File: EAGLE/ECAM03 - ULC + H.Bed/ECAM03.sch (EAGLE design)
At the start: 45 parts, among them J1 MODULAR TOOL, J2 FAN1, J3 FAN2, J4 FAN3, J5 S4B-PH-SM4, J6 SSR, J7 RINGLIGHT, J8 FTDI, J9 SPI, Q2 16MHz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

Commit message: BOMs complete for all FPD boards
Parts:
- C12: PARTNO (none) -> GRM188R61C106MA73D
- D1: PARTNO (none) -> B340A-13-F
- J2, J3, J4: PARTNO (none) -> 22232031
- J5: value S4B-PH-SM4 -> B4B-PH-SM4; PARTNO S4B-PH-SM4-TB(LF)(SN) -> B4B-PH-SM4-TB(LF)(SN)
- J6: PARTNO (none) -> 68000-102HLF
- J7: PARTNO (none) -> B5B-PH-SM4-TB(LF)(SN)
- J9: PARTNO (none) -> 67996-206HLF
- L1: PARTNO (none) -> BRL1608T6R8M
- R1: PARTNO (none) -> RC0603FR-0710KL
- R12: PARTNO (none) -> RC0603FR-0790K9L
- R15, R16: PARTNO (none) -> RC0603JR-070RL
- R6: PARTNO (none) -> RC0603FR-074K99L
- R7: PARTNO (none) -> RC1206FR-0710RL
- TB1: PARTNO (none) -> OSTTH020160
- U$1: PARTNO (none) -> *
- U3: PARTNO (none) -> MCP4725A0T-E/CH
- U4: PARTNO (none) -> MAX31855KASA+
- U5: PARTNO (none) -> NTR4003NT3G
- U6: PARTNO (none) -> SN74LVC1G02DBVR
- U8: PARTNO (none) -> AP3032KTR-G1

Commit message: BOMs finished, inventory sheet created.
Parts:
- R12: value 90K -> 90K9
- R2: PARTNO RC0603FR-07100RL -> RC0603FR-07120RL
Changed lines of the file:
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@@
 <part name="P+2" library="supply1" deviceset="+5V" device=""/>
 <part name="R2" library="TinWhiskers" deviceset="CPL-RES-0603-120-0.1W" device="" value="120R">
-<attribute name="PARTNO" value="RC0603FR-07100RL"/>
+<attribute name="PARTNO" value="RC0603FR-07120RL"/>
 </part>
 <part name="R3" library="TinWhiskers" deviceset="CPL-RES-0603-1K-0.1W" device="" value="1K">
@@
 <attribute name="PARTNO" value="RC1206FR-0710RL"/>
 </part>
-<part name="R12" library="TinWhiskers" deviceset="CPL-RES-0603-90K-0.1W" device="" value="90K">
+<part name="R12" library="TinWhiskers" deviceset="CPL-RES-0603-90K-0.1W" device="" value="90K9">
 <attribute name="PARTNO" value="RC0603FR-0790K9L"/>
 </part>

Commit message: Added decoupling caps to EFD01, ECAM02, rearranged parts for better fit, increased power trace width, updated BOM and database.
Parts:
- added C1, C10, C11, C2, C3, C9: 0.1uF, TinWhiskers:CPL-CAP-X5R-0603-0.1UF-35V
- U5: device TinWhiskers:CPL-MOSFET-NCH-SOT23 -> TinWhiskers:CPL-MOSFET-NCH-SOT23NTR4003N
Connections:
- net +3V3: now also C2.2
- net +5V: now also C1.2, C10.2, C11.2, C3.2, C9.2
- net GND: now also C1.1, C10.1, C11.1, C2.1, C3.1, C9.1; no longer U2.TAB
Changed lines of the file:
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@@
 <part name="SUPPLY10" library="TinWhiskers" deviceset="GND" device=""/>
 <part name="P+7" library="supply1" deviceset="+5V" device=""/>
-<part name="SUPPLY11" library="TinWhiskers" deviceset="GND" device=""/>
 <part name="SUPPLY12" library="TinWhiskers" deviceset="GND" device=""/>
 <part name="U1" library="TinWhiskers" deviceset="SP3485" device="">
@@
 <attribute name="PARTNO" value="22232031"/>
 </part>
-<part name="U5" library="TinWhiskers" deviceset="CPL-MOSFET-NCH-SOT23" device="" value="NTR4003NT3G">
+<part name="U5" library="TinWhiskers" deviceset="CPL-MOSFET-NCH-SOT23" device="NTR4003N" value="NTR4003NT3G">
 <attribute name="PARTNO" value="NTR4003NT3G"/>
 </part>
@@
 </part>
 <part name="SUPPLY5" library="TinWhiskers" deviceset="GND" device=""/>
+<part name="C1" library="TinWhiskers" deviceset="CPL-CAP-X5R-0603-0.1UF-35V" device="" value="0.1uF"/>
+<part name="SUPPLY19" library="TinWhiskers" deviceset="GND" device=""/>
+<part name="C2" library="TinWhiskers" deviceset="CPL-CAP-X5R-0603-0.1UF-35V" device="" value="0.1uF"/>
+<part name="+3V5" library="supply1" deviceset="+3V3" device=""/>
+<part name="SUPPLY20" library="TinWhiskers" deviceset="GND" device=""/>
+<part name="C3" library="TinWhiskers" deviceset="CPL-CAP-X5R-0603-0.1UF-35V" device="" value="0.1uF"/>
+<part name="SUPPLY21" library="TinWhiskers" deviceset="GND" device=""/>
+<part name="P+17" library="supply1" deviceset="+5V" device=""/>
+<part name="C9" library="TinWhiskers" deviceset="CPL-CAP-X5R-0603-0.1UF-35V" device="" value="0.1uF"/>
+<part name="SUPPLY24" library="TinWhiskers" deviceset="GND" device=""/>
+<part name="P+18" library="supply1" deviceset="+5V" device=""/>
+<part name="C10" library="TinWhiskers" deviceset="CPL-CAP-X5R-0603-0.1UF-35V" device="" value="0.1uF"/>
+<part name="SUPPLY25" library="TinWhiskers" deviceset="GND" device=""/>
+<part name="P+19" library="supply1" deviceset="+5V" device=""/>
+<part name="C11" library="TinWhiskers" deviceset="CPL-CAP-X5R-0603-0.1UF-35V" device="" value="0.1uF"/>
+<part name="SUPPLY28" library="TinWhiskers" deviceset="GND" device=""/>
+<part name="P+20" library="supply1" deviceset="+5V" device=""/>
 </parts>
 <sheets>
@@
 <attribute name="VALUE" x="355.6" y="236.22" size="1.778" layer="96"/>
 </instance>
-<instance part="SUPPLY11" gate="GND" x="320.04" y="175.26"/>
 <instance part="SUPPLY12" gate="GND" x="347.98" y="175.26"/>
 <instance part="U1" gate="G$1" x="210.82" y="116.84" smashed="yes">
@@
 <attribute name="PARTNO" x="233.68" y="101.6" size="2.54" layer="96" ratio="10" display="off"/>
 </instance>
-<instance part="+3V2" gate="G$1" x="233.68" y="142.24"/>
-<instance part="+3V3" gate="G$1" x="226.06" y="142.24"/>
+<instance part="+3V2" gate="G$1" x="233.68" y="142.24" smashed="yes">
+<attribute name="VALUE" x="231.14" y="142.24" size="1.778" layer="96"/>
+</instance>
+<instance part="+3V3" gate="G$1" x="226.06" y="142.24" smashed="yes">
+<attribute name="VALUE" x="223.52" y="142.24" size="1.778" layer="96"/>
+</instance>
 <instance part="SUPPLY2" gate="GND" x="233.68" y="91.44"/>
 <instance part="SUPPLY3" gate="GND" x="226.06" y="91.44"/>
@@
 <instance part="SUPPLY5" gate="GND" x="132.08" y="38.1" smashed="yes">
 <attribute name="VALUE" x="130.175" y="34.925" size="1.778" layer="96"/>
+</instance>
+<instance part="C1" gate="G$1" x="279.4" y="220.98" smashed="yes" rot="R90">
+<attribute name="NAME" x="279.019" y="214.884" size="1.778" layer="95" rot="R90"/>
+<attribute name="VALUE" x="281.559" y="211.582" size="1.778" layer="96" rot="R90"/>
+</instance>
+<instance part="SUPPLY19" gate="GND" x="279.4" y="210.82"/>
+<instance part="C2" gate="G$1" x="195.58" y="104.14" smashed="yes" rot="R90">
+<attribute name="NAME" x="195.199" y="98.044" size="1.778" layer="95" rot="R90"/>
+<attribute name="VALUE" x="197.739" y="94.742" size="1.778" layer="96" rot="R90"/>
+</instance>
+<instance part="+3V5" gate="G$1" x="195.58" y="111.76" smashed="yes">
+<attribute name="VALUE" x="193.04" y="111.76" size="1.778" layer="96"/>
+</instance>
+<instance part="SUPPLY20" gate="GND" x="195.58" y="93.98"/>
+<instance part="C3" gate="G$1" x="15.24" y="55.88" smashed="yes" rot="R90">
+<attribute name="NAME" x="14.859" y="49.784" size="1.778" layer="95" rot="R90"/>
+<attribute name="VALUE" x="17.399" y="46.482" size="1.778" layer="96" rot="R90"/>
+</instance>
+<instance part="SUPPLY21" gate="GND" x="15.24" y="45.72"/>
+<instance part="P+17" gate="1" x="15.24" y="63.5" smashed="yes">
+<attribute name="VALUE" x="12.7" y="63.5" size="1.778" layer="96"/>
+</instance>
+<instance part="C9" gate="G$1" x="81.28" y="55.88" smashed="yes" rot="R90">
+<attribute name="NAME" x="80.899" y="49.784" size="1.778" layer="95" rot="R90"/>
+<attribute name="VALUE" x="83.439" y="46.482" size="1.778" layer="96" rot="R90"/>
+</instance>
+<instance part="SUPPLY24" gate="GND" x="81.28" y="45.72"/>
+<instance part="P+18" gate="1" x="81.28" y="63.5" smashed="yes">
+<attribute name="VALUE" x="78.74" y="63.5" size="1.778" layer="96"/>
+</instance>
+<instance part="C10" gate="G$1" x="193.04" y="58.42" smashed="yes" rot="R90">
+<attribute name="NAME" x="192.659" y="51.308" size="1.778" layer="95" rot="R90"/>
+<attribute name="VALUE" x="195.199" y="49.022" size="1.778" layer="96" rot="R90"/>
+</instance>
+<instance part="SUPPLY25" gate="GND" x="193.04" y="48.26"/>
+<instance part="P+19" gate="1" x="193.04" y="66.04" smashed="yes">
+<attribute name="VALUE" x="190.5" y="66.04" size="1.778" layer="96"/>
+</instance>
+<instance part="C11" gate="G$1" x="279.4" y="50.8" smashed="yes" rot="R90">
+<attribute name="NAME" x="279.019" y="43.942" size="1.778" layer="95" rot="R90"/>
+<attribute name="VALUE" x="281.559" y="41.402" size="1.778" layer="96" rot="R90"/>
+</instance>
+<instance part="SUPPLY28" gate="GND" x="279.4" y="40.64"/>
+<instance part="P+20" gate="1" x="279.4" y="58.42" smashed="yes">
+<attribute name="VALUE" x="276.86" y="58.42" size="1.778" layer="96"/>
 </instance>
 </instances>
@@
 </segment>
 <segment>
-<pinref part="U2" gate="G$1" pin="TAB"/>
-<wire x1="322.58" y1="180.34" x2="320.04" y2="180.34" width="0.1524" layer="91"/>
-<wire x1="320.04" y1="180.34" x2="320.04" y2="177.8" width="0.1524" layer="91"/>
-<pinref part="SUPPLY11" gate="GND" pin="GND"/>
-</segment>
-<segment>
 <wire x1="261.62" y1="119.38" x2="259.08" y2="119.38" width="0.1524" layer="91"/>
 <wire x1="259.08" y1="119.38" x2="259.08" y2="106.68" width="0.1524" layer="91"/>
@@
 <wire x1="119.38" y1="55.88" x2="132.08" y2="55.88" width="0.1524" layer="91"/>
 <wire x1="132.08" y1="55.88" x2="132.08" y2="40.64" width="0.1524" layer="91"/>
+</segment>
+<segment>
+<pinref part="C1" gate="G$1" pin="1"/>
+<pinref part="SUPPLY19" gate="GND" pin="GND"/>
+<wire x1="279.4" y1="215.9" x2="279.4" y2="213.36" width="0.1524" layer="91"/>
+</segment>
+<segment>
+<pinref part="C2" gate="G$1" pin="1"/>
+<pinref part="SUPPLY20" gate="GND" pin="GND"/>
+<wire x1="195.58" y1="99.06" x2="195.58" y2="96.52" width="0.1524" layer="91"/>
+</segment>
+<segment>
+<pinref part="C3" gate="G$1" pin="1"/>
+<pinref part="SUPPLY21" gate="GND" pin="GND"/>
+<wire x1="15.24" y1="50.8" x2="15.24" y2="48.26" width="0.1524" layer="91"/>
+</segment>
+<segment>
+<pinref part="C9" gate="G$1" pin="1"/>
+<pinref part="SUPPLY24" gate="GND" pin="GND"/>
+<wire x1="81.28" y1="50.8" x2="81.28" y2="48.26" width="0.1524" layer="91"/>
+</segment>
+<segment>
+<pinref part="C10" gate="G$1" pin="1"/>
+<pinref part="SUPPLY25" gate="GND" pin="GND"/>
+<wire x1="193.04" y1="53.34" x2="193.04" y2="50.8" width="0.1524" layer="91"/>
+</segment>
+<segment>
+<pinref part="C11" gate="G$1" pin="1"/>
+<pinref part="SUPPLY28" gate="GND" pin="GND"/>
+<wire x1="279.4" y1="45.72" x2="279.4" y2="43.18" width="0.1524" layer="91"/>
 </segment>
 </net>
@@
 <wire x1="299.72" y1="226.06" x2="297.18" y2="226.06" width="0.1524" layer="91"/>
 <wire x1="297.18" y1="226.06" x2="297.18" y2="228.6" width="0.1524" layer="91"/>
+<pinref part="C1" gate="G$1" pin="2"/>
+<wire x1="297.18" y1="226.06" x2="279.4" y2="226.06" width="0.1524" layer="91"/>
+<wire x1="279.4" y1="226.06" x2="279.4" y2="223.52" width="0.1524" layer="91"/>
+<junction x="297.18" y="226.06"/>
 </segment>
 <segment>
@@
 <wire x1="149.86" y1="200.66" x2="149.86" y2="203.2" width="0.1524" layer="91"/>
 <pinref part="P+16" gate="1" pin="+5V"/>
+</segment>
+<segment>
+<pinref part="C3" gate="G$1" pin="2"/>
+<wire x1="15.24" y1="60.96" x2="15.24" y2="58.42" width="0.1524" layer="91"/>
+<pinref part="P+17" gate="1" pin="+5V"/>
+</segment>
+<segment>
+<pinref part="C9" gate="G$1" pin="2"/>
+<wire x1="81.28" y1="60.96" x2="81.28" y2="58.42" width="0.1524" layer="91"/>
+<pinref part="P+18" gate="1" pin="+5V"/>
+</segment>
+<segment>
+<pinref part="C10" gate="G$1" pin="2"/>
+<wire x1="193.04" y1="63.5" x2="193.04" y2="60.96" width="0.1524" layer="91"/>
+<pinref part="P+19" gate="1" pin="+5V"/>
+</segment>
+<segment>
+<pinref part="C11" gate="G$1" pin="2"/>
+<wire x1="279.4" y1="55.88" x2="279.4" y2="53.34" width="0.1524" layer="91"/>
+<pinref part="P+20" gate="1" pin="+5V"/>
 </segment>
 </net>
@@
 <pinref part="+3V4" gate="G$1" pin="+3V3"/>
 </segment>
+<segment>
+<pinref part="+3V5" gate="G$1" pin="+3V3"/>
+<pinref part="C2" gate="G$1" pin="2"/>
+<wire x1="195.58" y1="109.22" x2="195.58" y2="106.68" width="0.1524" layer="91"/>
+</segment>
 </net>
 <net name="DTR1" class="0">
@@
 <pinref part="U2" gate="G$1" pin="PB0"/>
 <wire x1="322.58" y1="231.14" x2="312.42" y2="231.14" width="0.1524" layer="91"/>
-<label x="312.42" y="231.14" size="1.778" layer="95"/>
-</segment>
-<segment>
+<label x="307.34" y="231.14" size="1.778" layer="95"/>
+</segment>
+<segment>

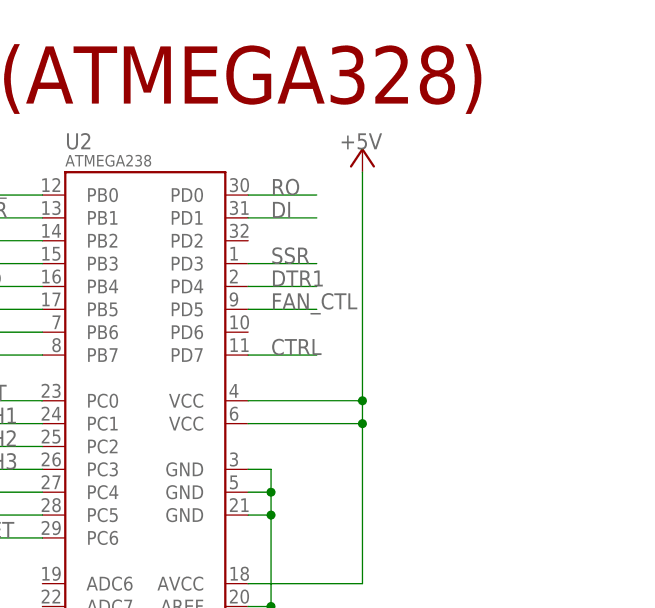
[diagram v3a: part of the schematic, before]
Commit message: Made REV 2 modifications, including increasing width of power traces, adding vias to power traces, and addition of LEDs to all modular tools. Catch diodes added to ESOL01 board to prevent coils from creating problems "upstream"
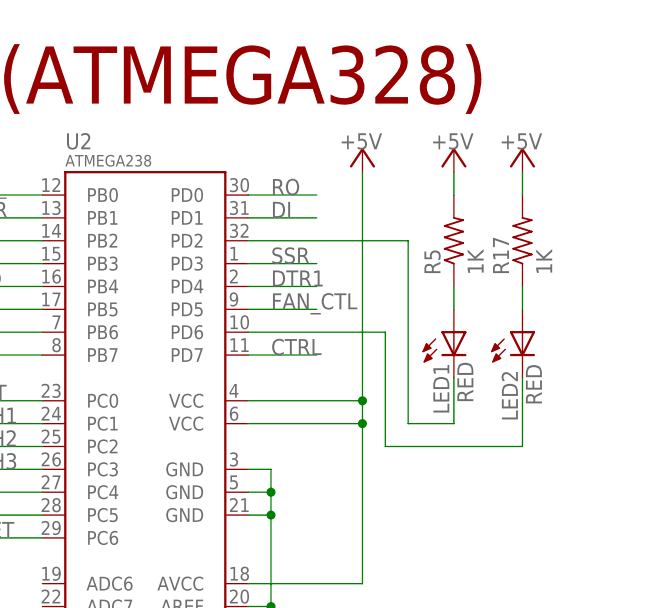
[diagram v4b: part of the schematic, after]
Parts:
- added LED1, LED2: RED, TinWhiskers:CPL-LED-0603-RED
- added R17, R5: 1K, TinWhiskers:CPL-RES-0603-1K-0.1W
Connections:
- new net N$1: LED2.A, R17.1
- new net N$2: LED1.A, R5.1
- new net N$3: LED1.C, U2.PD2
- new net N$4: LED2.C, U2.PD6
- net +5V: now also R17.2, R5.2
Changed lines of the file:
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@@
 <part name="SUPPLY28" library="TinWhiskers" deviceset="GND" device=""/>
 <part name="P+20" library="supply1" deviceset="+5V" device=""/>
+<part name="P+21" library="supply1" deviceset="+5V" device=""/>
+<part name="P+22" library="supply1" deviceset="+5V" device=""/>
+<part name="R5" library="TinWhiskers" deviceset="CPL-RES-0603-1K-0.1W" device="" value="1K"/>
+<part name="R17" library="TinWhiskers" deviceset="CPL-RES-0603-1K-0.1W" device="" value="1K"/>
+<part name="LED1" library="TinWhiskers" deviceset="CPL-LED-0603-RED" device="" value="RED"/>
+<part name="LED2" library="TinWhiskers" deviceset="CPL-LED-0603-RED" device="" value="RED"/>
 </parts>
 <sheets>
@@
 <attribute name="VALUE" x="276.86" y="58.42" size="1.778" layer="96"/>
 </instance>
+<instance part="P+21" gate="1" x="375.92" y="236.22" smashed="yes">
+<attribute name="VALUE" x="373.38" y="236.22" size="1.778" layer="96"/>
+</instance>
+<instance part="P+22" gate="1" x="368.3" y="236.22" smashed="yes">
+<attribute name="VALUE" x="365.76" y="236.22" size="1.778" layer="96"/>
+</instance>
+<instance part="R5" gate="G$1" x="368.3" y="226.06" rot="R90"/>
+<instance part="R17" gate="G$1" x="375.92" y="226.06" rot="R90"/>
+<instance part="LED1" gate="G$1" x="368.3" y="215.9" smashed="yes">
+<attribute name="NAME" x="367.792" y="206.756" size="1.778" layer="95" rot="R90"/>
+<attribute name="VALUE" x="370.459" y="208.026" size="1.778" layer="96" rot="R90"/>
+</instance>
+<instance part="LED2" gate="G$1" x="375.92" y="215.9" smashed="yes">
+<attribute name="NAME" x="375.412" y="205.994" size="1.778" layer="95" rot="R90"/>
+<attribute name="VALUE" x="378.079" y="207.772" size="1.778" layer="96" rot="R90"/>
+</instance>
 </instances>
 <busses>
@@
 <pinref part="P+20" gate="1" pin="+5V"/>
 </segment>
+<segment>
+<pinref part="P+22" gate="1" pin="+5V"/>
+<pinref part="R5" gate="G$1" pin="2"/>
+<wire x1="368.3" y1="233.68" x2="368.3" y2="231.14" width="0.1524" layer="91"/>
+</segment>
+<segment>
+<pinref part="P+21" gate="1" pin="+5V"/>
+<pinref part="R17" gate="G$1" pin="2"/>
+<wire x1="375.92" y1="233.68" x2="375.92" y2="231.14" width="0.1524" layer="91"/>
+</segment>
 </net>
 <net name="RO" class="0">
@@
 </segment>
 </net>
+<net name="N$1" class="0">
+<segment>
+<pinref part="R17" gate="G$1" pin="1"/>
+<pinref part="LED2" gate="G$1" pin="A"/>
+<wire x1="375.92" y1="220.98" x2="375.92" y2="218.44" width="0.1524" layer="91"/>
+</segment>
+</net>
+<net name="N$2" class="0">
+<segment>
+<pinref part="R5" gate="G$1" pin="1"/>
+<pinref part="LED1" gate="G$1" pin="A"/>
+<wire x1="368.3" y1="220.98" x2="368.3" y2="218.44" width="0.1524" layer="91"/>
+</segment>
+</net>
+<net name="N$3" class="0">
+<segment>
+<pinref part="U2" gate="G$1" pin="PD2"/>
+<wire x1="345.44" y1="226.06" x2="363.22" y2="226.06" width="0.1524" layer="91"/>
+<wire x1="363.22" y1="226.06" x2="363.22" y2="205.74" width="0.1524" layer="91"/>
+<wire x1="363.22" y1="205.74" x2="368.3" y2="205.74" width="0.1524" layer="91"/>
+<pinref part="LED1" gate="G$1" pin="C"/>
+<wire x1="368.3" y1="205.74" x2="368.3" y2="210.82" width="0.1524" layer="91"/>
+</segment>
+</net>
+<net name="N$4" class="0">
+<segment>
+<pinref part="LED2" gate="G$1" pin="C"/>
+<wire x1="375.92" y1="210.82" x2="375.92" y2="203.2" width="0.1524" layer="91"/>
+<wire x1="375.92" y1="203.2" x2="360.68" y2="203.2" width="0.1524" layer="91"/>
+<pinref part="U2" gate="G$1" pin="PD6"/>
+<wire x1="360.68" y1="203.2" x2="360.68" y2="215.9" width="0.1524" layer="91"/>
+<wire x1="360.68" y1="215.9" x2="345.44" y2="215.9" width="0.1524" layer="91"/>
+</segment>
+</net>
